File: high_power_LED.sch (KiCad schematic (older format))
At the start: 14 parts

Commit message: Annotate sheets and assign symbols
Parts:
- removed J?: TH-, symbol Connector:Conn_01x01_Female
- D2, D3, D4: renamed from D?; footprint (none) -> extraFootprints:Cree-XLamp-MX6
- H3, H4: renamed from H?; footprint (none) -> MountingHole:MountingHole_2.7mm_M2.5_ISO14580
- HS1: renamed from HS?; footprint (none) -> Heatsink:Heatsink_AAVID_573300D00010G_TO-263
- J15, J16: renamed from J?; footprint (none) -> Connector_PinHeader_2.54mm:PinHeader_1x01_P2.54mm_Vertical
- J17: renamed from J?; value TH+ -> TH; footprint (none) -> Connector_Molex:Molex_PicoBlade_53047-0210_1x02_P1.25mm_Vertical; symbol Connector:Conn_01x01_Female -> Connector:Conn_01x02_Female
- JP3, JP4, JP5: renamed from JP?; footprint (none) -> Jumper:SolderJumper-2_P1.3mm_Open_TrianglePad1.0x1.5mm
- TH1: renamed from TH?; footprint (none) -> Resistor_SMD:R_0603_1608Metric
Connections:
- net at TH1.2: now also J17.2 (Pin_2)
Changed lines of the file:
@@
 $EndDescr
 $Comp
-L Device:LED_PAD D?
+L Device:LED_PAD D2
 U 1 1 602B1BC1
 P 4450 2350
-F 0 "D?" V 4496 2493 50  0000 L CNN
+F 0 "D2" V 4496 2493 50  0000 L CNN
 F 1 "LED_PAD" V 4350 2450 50  0000 L CNN
-F 2 "" H 4450 2350 50  0001 C CNN
+F 2 "extraFootprints:Cree-XLamp-MX6" H 4450 2350 50  0001 C CNN
 F 3 "~" H 4450 2350 50  0001 C CNN
 	1    4450 2350
@@
 $EndComp
 $Comp
-L Device:LED_PAD D?
+L Device:LED_PAD D3
 U 1 1 602B2FF1
 P 4450 2750
-F 0 "D?" V 4496 2893 50  0000 L CNN
+F 0 "D3" V 4496 2893 50  0000 L CNN
 F 1 "LED_PAD" V 4350 2850 50  0000 L CNN
-F 2 "" H 4450 2750 50  0001 C CNN
+F 2 "extraFootprints:Cree-XLamp-MX6" H 4450 2750 50  0001 C CNN
 F 3 "~" H 4450 2750 50  0001 C CNN
 	1    4450 2750
@@
 $EndComp
 $Comp
-L Device:LED_PAD D?
+L Device:LED_PAD D4
 U 1 1 602B35BF
 P 4450 3150
-F 0 "D?" V 4496 3293 50  0000 L CNN
+F 0 "D4" V 4496 3293 50  0000 L CNN
 F 1 "LED_PAD" V 4350 3250 50  0000 L CNN
-F 2 "" H 4450 3150 50  0001 C CNN
+F 2 "extraFootprints:Cree-XLamp-MX6" H 4450 3150 50  0001 C CNN
 F 3 "~" H 4450 3150 50  0001 C CNN
 	1    4450 3150
@@
 $EndComp
 $Comp
-L Jumper:SolderJumper_2_Open JP?
+L Jumper:SolderJumper_2_Open JP4
 U 1 1 602B419C
 P 3850 2750
-F 0 "JP?" V 3850 2662 50  0000 R CNN
+F 0 "JP4" V 3850 2662 50  0000 R CNN
 F 1 "SolderJumper_2_Open" V 3895 2662 50  0001 R CNN
-F 2 "" H 3850 2750 50  0001 C CNN
+F 2 "Jumper:SolderJumper-2_P1.3mm_Open_TrianglePad1.0x1.5mm" H 3850 2750 50  0001 C CNN
 F 3 "~" H 3850 2750 50  0001 C CNN
 	1    3850 2750
@@
 $EndComp
 $Comp
-L Jumper:SolderJumper_2_Open JP?
+L Jumper:SolderJumper_2_Open JP5
 U 1 1 602B5BED
 P 3850 3150
-F 0 "JP?" V 3850 3062 50  0000 R CNN
+F 0 "JP5" V 3850 3062 50  0000 R CNN
 F 1 "SolderJumper_2_Open" V 3895 3062 50  0001 R CNN
-F 2 "" H 3850 3150 50  0001 C CNN
+F 2 "Jumper:SolderJumper-2_P1.3mm_Open_TrianglePad1.0x1.5mm" H 3850 3150 50  0001 C CNN
 F 3 "~" H 3850 3150 50  0001 C CNN
 	1    3850 3150
@@
 Connection ~ 3850 2950
 $Comp
-L Jumper:SolderJumper_2_Open JP?
+L Jumper:SolderJumper_2_Open JP3
 U 1 1 602B6896
 P 3850 2350
-F 0 "JP?" V 3850 2262 50  0000 R CNN
+F 0 "JP3" V 3850 2262 50  0000 R CNN
 F 1 "SolderJumper_2_Open" V 3895 2262 50  0001 R CNN
-F 2 "" H 3850 2350 50  0001 C CNN
+F 2 "Jumper:SolderJumper-2_P1.3mm_Open_TrianglePad1.0x1.5mm" H 3850 2350 50  0001 C CNN
 F 3 "~" H 3850 2350 50  0001 C CNN
 	1    3850 2350
@@
 you can skip LEDs by soldering it's jumper pad
 $Comp
-L Mechanical:Heatsink_Pad HS?
+L Mechanical:Heatsink_Pad HS1
 U 1 1 602B8592
 P 4850 2600
-F 0 "HS?" H 4991 2639 50  0000 L CNN
+F 0 "HS1" H 4991 2639 50  0000 L CNN
 F 1 "Heatsink_Pad" H 4700 2750 50  0000 L CNN
-F 2 "" H 4862 2550 50  0001 C CNN
+F 2 "Heatsink:Heatsink_AAVID_573300D00010G_TO-263" H 4862 2550 50  0001 C CNN
 F 3 "~" H 4862 2550 50  0001 C CNN
 	1    4850 2600
@@
 Connection ~ 4450 3350
 $Comp
-L Device:Thermistor TH?
+L Device:Thermistor TH1
 U 1 1 602BA374
 P 5500 2250
-F 0 "TH?" H 5605 2296 50  0000 L CNN
+F 0 "TH1" H 5605 2296 50  0000 L CNN
 F 1 "Thermistor" H 5605 2205 50  0000 L CNN
-F 2 "" H 5500 2250 50  0001 C CNN
+F 2 "Resistor_SMD:R_0603_1608Metric" H 5500 2250 50  0001 C CNN
 F 3 "~" H 5500 2250 50  0001 C CNN
 	1    5500 2250
@@
 	4500 2050 4450 2050
 $Comp
-L Connector:Conn_01x01_Female J?
+L Connector:Conn_01x01_Female J15
 U 1 1 602C1EF5
 P 4700 2050
-F 0 "J?" H 4700 2100 50  0000 R CNN
+F 0 "J15" H 4700 2100 50  0000 R CNN
 F 1 "Anode" H 4950 2050 50  0000 R CNN
-F 2 "" H 4700 2050 50  0001 C CNN
+F 2 "Connector_PinHeader_2.54mm:PinHeader_1x01_P2.54mm_Vertical" H 4700 2050 50  0001 C CNN
 F 3 "~" H 4700 2050 50  0001 C CNN
 	1    4700 2050
@@
 $EndComp
 $Comp
-L Connector:Conn_01x01_Female J?
-U 1 1 602C273F
-P 6400 2200
-F 0 "J?" H 6400 2250 50  0000 R CNN
-F 1 "TH+" H 6600 2200 50  0000 R CNN
-F 2 "" H 6400 2200 50  0001 C CNN
-F 3 "~" H 6400 2200 50  0001 C CNN
-	1    6400 2200
-	1    0    0    -1
-$EndComp
-$Comp
-L Connector:Conn_01x01_Female J?
-U 1 1 602C2960
-P 6400 2300
-F 0 "J?" H 6400 2350 50  0000 R CNN
-F 1 "TH-" H 6600 2300 50  0000 R CNN
-F 2 "" H 6400 2300 50  0001 C CNN
-F 3 "~" H 6400 2300 50  0001 C CNN
-	1    6400 2300
-	1    0    0    -1
-$EndComp
-$Comp
-L Connector:Conn_01x01_Female J?
+L Connector:Conn_01x01_Female J16
 U 1 1 602C2C18
 P 4700 3450
-F 0 "J?" H 4700 3500 50  0000 R CNN
+F 0 "J16" H 4700 3500 50  0000 R CNN
 F 1 "Cathode" H 5050 3450 50  0000 R CNN
-F 2 "" H 4700 3450 50  0001 C CNN
+F 2 "Connector_PinHeader_2.54mm:PinHeader_1x01_P2.54mm_Vertical" H 4700 3450 50  0001 C CNN
 F 3 "~" H 4700 3450 50  0001 C CNN
 	1    4700 3450
@@
 $EndComp
 $Comp
-L Mechanical:MountingHole H?
+L Mechanical:MountingHole H3
 U 1 1 602C46DF
 P 3000 2100
-F 0 "H?" H 3100 2146 50  0000 L CNN
+F 0 "H3" H 3100 2146 50  0000 L CNN
 F 1 "MountingHole" H 3100 2055 50  0000 L CNN
-F 2 "" H 3000 2100 50  0001 C CNN
+F 2 "MountingHole:MountingHole_2.7mm_M2.5_ISO14580" H 3000 2100 50  0001 C CNN
 F 3 "~" H 3000 2100 50  0001 C CNN
 	1    3000 2100
@@
 $EndComp
 $Comp
-L Mechanical:MountingHole H?
+L Mechanical:MountingHole H4
 U 1 1 602C4749
 P 3000 2350
-F 0 "H?" H 3100 2396 50  0000 L CNN
+F 0 "H4" H 3100 2396 50  0000 L CNN
 F 1 "MountingHole" H 3100 2305 50  0000 L CNN
-F 2 "" H 3000 2350 50  0001 C CNN
+F 2 "MountingHole:MountingHole_2.7mm_M2.5_ISO14580" H 3000 2350 50  0001 C CNN
 F 3 "~" H 3000 2350 50  0001 C CNN
 	1    3000 2350
@@
 Text Notes 3750 1900 0    50   ~ 0
 high power LED
+$Comp
+L Connector:Conn_01x02_Female J17
+U 1 1 602C273F
+P 6400 2200
+F 0 "J17" H 6450 2300 50  0000 R CNN
+F 1 "TH" H 6550 2150 50  0000 R CNN
+F 2 "Connector_Molex:Molex_PicoBlade_53047-0210_1x02_P1.25mm_Vertical" H 6400 2200 50  0001 C CNN
+F 3 "~" H 6400 2200 50  0001 C CNN
+	1    6400 2200
+	1    0    0    -1
+$EndComp
 $EndSCHEMATC

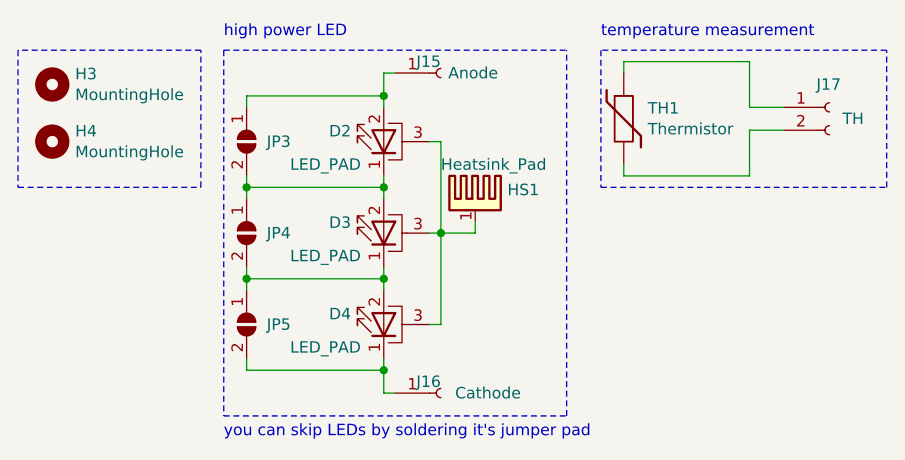
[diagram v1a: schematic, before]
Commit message: Split project into individual projects and reannotate sheets
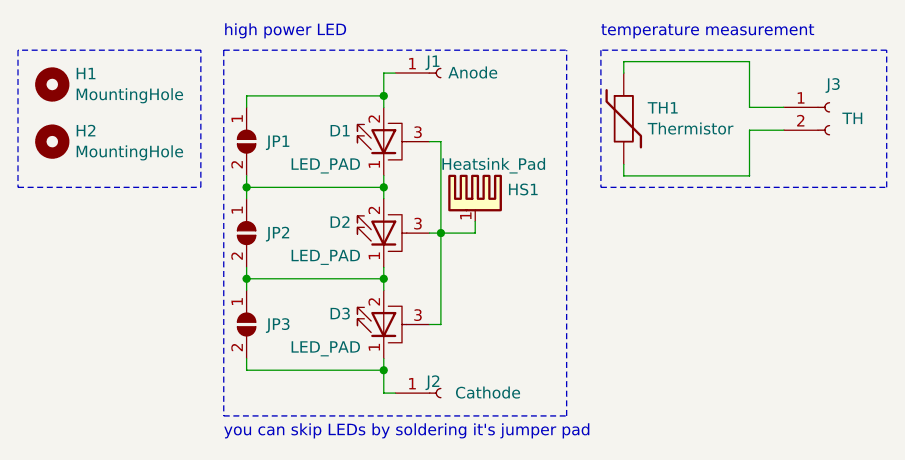
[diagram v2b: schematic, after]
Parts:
- renumbered D2 to D1, D3 to D2, D4 to D3, H3 to H1, H4 to H2, J15 to J1, J16 to J2, J17 to J3, JP3 to JP1, JP4 to JP2, JP5 to JP3
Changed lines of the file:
@@
 $Descr A4 11693 8268
 encoding utf-8
-Sheet 4 4
+Sheet 1 1
 Title ""
 Date ""
@@
 $EndDescr
 $Comp
-L Device:LED_PAD D2
+L Device:LED_PAD D1
 U 1 1 602B1BC1
 P 4450 2350
-F 0 "D2" V 4496 2493 50  0000 L CNN
+F 0 "D1" V 4496 2493 50  0000 L CNN
 F 1 "LED_PAD" V 4350 2450 50  0000 L CNN
 F 2 "extraFootprints:Cree-XLamp-MX6" H 4450 2350 50  0001 C CNN
@@
 $EndComp
 $Comp
-L Device:LED_PAD D3
+L Device:LED_PAD D2
 U 1 1 602B2FF1
 P 4450 2750
-F 0 "D3" V 4496 2893 50  0000 L CNN
+F 0 "D2" V 4496 2893 50  0000 L CNN
 F 1 "LED_PAD" V 4350 2850 50  0000 L CNN
 F 2 "extraFootprints:Cree-XLamp-MX6" H 4450 2750 50  0001 C CNN
@@
 $EndComp
 $Comp
-L Device:LED_PAD D4
+L Device:LED_PAD D3
 U 1 1 602B35BF
 P 4450 3150
-F 0 "D4" V 4496 3293 50  0000 L CNN
+F 0 "D3" V 4496 3293 50  0000 L CNN
 F 1 "LED_PAD" V 4350 3250 50  0000 L CNN
 F 2 "extraFootprints:Cree-XLamp-MX6" H 4450 3150 50  0001 C CNN
@@
 $EndComp
 $Comp
-L Jumper:SolderJumper_2_Open JP4
+L Jumper:SolderJumper_2_Open JP2
 U 1 1 602B419C
 P 3850 2750
-F 0 "JP4" V 3850 2662 50  0000 R CNN
+F 0 "JP2" V 3850 2662 50  0000 R CNN
 F 1 "SolderJumper_2_Open" V 3895 2662 50  0001 R CNN
 F 2 "Jumper:SolderJumper-2_P1.3mm_Open_TrianglePad1.0x1.5mm" H 3850 2750 50  0001 C CNN
@@
 $EndComp
 $Comp
-L Jumper:SolderJumper_2_Open JP5
+L Jumper:SolderJumper_2_Open JP3
 U 1 1 602B5BED
 P 3850 3150
-F 0 "JP5" V 3850 3062 50  0000 R CNN
+F 0 "JP3" V 3850 3062 50  0000 R CNN
 F 1 "SolderJumper_2_Open" V 3895 3062 50  0001 R CNN
 F 2 "Jumper:SolderJumper-2_P1.3mm_Open_TrianglePad1.0x1.5mm" H 3850 3150 50  0001 C CNN
@@
 Connection ~ 3850 2950
 $Comp
-L Jumper:SolderJumper_2_Open JP3
+L Jumper:SolderJumper_2_Open JP1
 U 1 1 602B6896
 P 3850 2350
-F 0 "JP3" V 3850 2262 50  0000 R CNN
+F 0 "JP1" V 3850 2262 50  0000 R CNN
 F 1 "SolderJumper_2_Open" V 3895 2262 50  0001 R CNN
 F 2 "Jumper:SolderJumper-2_P1.3mm_Open_TrianglePad1.0x1.5mm" H 3850 2350 50  0001 C CNN
@@
 	4500 2050 4450 2050
 $Comp
-L Connector:Conn_01x01_Female J15
+L Connector:Conn_01x01_Female J1
 U 1 1 602C1EF5
 P 4700 2050
-F 0 "J15" H 4700 2100 50  0000 R CNN
+F 0 "J1" H 4700 2100 50  0000 R CNN
 F 1 "Anode" H 4950 2050 50  0000 R CNN
 F 2 "Connector_PinHeader_2.54mm:PinHeader_1x01_P2.54mm_Vertical" H 4700 2050 50  0001 C CNN
@@
 $EndComp
 $Comp
-L Connector:Conn_01x01_Female J16
+L Connector:Conn_01x01_Female J2
 U 1 1 602C2C18
 P 4700 3450
-F 0 "J16" H 4700 3500 50  0000 R CNN
+F 0 "J2" H 4700 3500 50  0000 R CNN
 F 1 "Cathode" H 5050 3450 50  0000 R CNN
 F 2 "Connector_PinHeader_2.54mm:PinHeader_1x01_P2.54mm_Vertical" H 4700 3450 50  0001 C CNN
@@
 $EndComp
 $Comp
-L Mechanical:MountingHole H3
+L Mechanical:MountingHole H1
 U 1 1 602C46DF
 P 3000 2100
-F 0 "H3" H 3100 2146 50  0000 L CNN
+F 0 "H1" H 3100 2146 50  0000 L CNN
 F 1 "MountingHole" H 3100 2055 50  0000 L CNN
 F 2 "MountingHole:MountingHole_2.7mm_M2.5_ISO14580" H 3000 2100 50  0001 C CNN
@@
 $EndComp
 $Comp
-L Mechanical:MountingHole H4
+L Mechanical:MountingHole H2
 U 1 1 602C4749
 P 3000 2350
-F 0 "H4" H 3100 2396 50  0000 L CNN
+F 0 "H2" H 3100 2396 50  0000 L CNN
 F 1 "MountingHole" H 3100 2305 50  0000 L CNN
 F 2 "MountingHole:MountingHole_2.7mm_M2.5_ISO14580" H 3000 2350 50  0001 C CNN
@@
 high power LED
 $Comp
-L Connector:Conn_01x02_Female J17
+L Connector:Conn_01x02_Female J3
 U 1 1 602C273F
 P 6400 2200
-F 0 "J17" H 6450 2300 50  0000 R CNN
+F 0 "J3" H 6450 2300 50  0000 R CNN
 F 1 "TH" H 6550 2150 50  0000 R CNN
 F 2 "Connector_Molex:Molex_PicoBlade_53047-0210_1x02_P1.25mm_Vertical" H 6400 2200 50  0001 C CNN

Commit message: Finish high power led pcb
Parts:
- removed J2: Cathode, Connector_PinHeader_2.54mm:PinHeader_1x01_P2.54mm_Vertical, symbol Connector:Conn_01x01_Female
- J1: value Anode -> LED; footprint Connector_PinHeader_2.54mm:PinHeader_1x01_P2.54mm_Vertical -> Connector_PinHeader_2.54mm:PinHeader_1x02_P2.54mm_Vertical; symbol Connector:Conn_01x01_Female -> Connector:Conn_01x02_Female
- renumbered J3 to J2
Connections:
- net Anode: now reaches D1.2 (A), J1.1 (Pin_1), JP1.1 (A)
- net Cathode: now reaches D3.1 (K), JP3.2 (B)
- net Cathode: now also J1.2 (Pin_2)
- net TH+: now reaches J2.1 (Pin_1), TH1.1
- net TH-: now reaches J2.2 (Pin_2), TH1.2
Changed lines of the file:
@@
 $EndComp
-Wire Wire Line
-	4450 3450 4500 3450
 Wire Wire Line
 	5500 2450 5500 2500
@@
 	4500 2050 4450 2050
 $Comp
-L Connector:Conn_01x01_Female J1
+L Connector:Conn_01x02_Female J1
 U 1 1 602C1EF5
-P 4700 2050
-F 0 "J1" H 4700 2100 50  0000 R CNN
-F 1 "Anode" H 4950 2050 50  0000 R CNN
-F 2 "Connector_PinHeader_2.54mm:PinHeader_1x01_P2.54mm_Vertical" H 4700 2050 50  0001 C CNN
-F 3 "~" H 4700 2050 50  0001 C CNN
-	1    4700 2050
-	1    0    0    -1
-$EndComp
-$Comp
-L Connector:Conn_01x01_Female J2
-U 1 1 602C2C18
-P 4700 3450
-F 0 "J2" H 4700 3500 50  0000 R CNN
-F 1 "Cathode" H 5050 3450 50  0000 R CNN
-F 2 "Connector_PinHeader_2.54mm:PinHeader_1x01_P2.54mm_Vertical" H 4700 3450 50  0001 C CNN
-F 3 "~" H 4700 3450 50  0001 C CNN
-	1    4700 3450
+P 5100 3350
+F 0 "J1" H 5100 3400 50  0000 R CNN
+F 1 "LED" V 5200 3350 50  0000 R CNN
+F 2 "Connector_PinHeader_2.54mm:PinHeader_1x02_P2.54mm_Vertical" H 5100 3350 50  0001 C CNN
+F 3 "~" H 5100 3350 50  0001 C CNN
+	1    5100 3350
 	1    0    0    -1
 $EndComp
@@
 high power LED
 $Comp
-L Connector:Conn_01x02_Female J3
+L Connector:Conn_01x02_Female J2
 U 1 1 602C273F
 P 6400 2200
-F 0 "J3" H 6450 2300 50  0000 R CNN
+F 0 "J2" H 6450 2300 50  0000 R CNN
 F 1 "TH" H 6550 2150 50  0000 R CNN
 F 2 "Connector_Molex:Molex_PicoBlade_53047-0210_1x02_P1.25mm_Vertical" H 6400 2200 50  0001 C CNN
@@
 	1    0    0    -1
 $EndComp
+Text Label 4500 2050 0    50   ~ 0
+Anode
+Text Label 4850 3450 2    50   ~ 0
+Cathode
+Wire Wire Line
+	4450 3450 4900 3450
+Wire Wire Line
+	4900 3350 4850 3350
+Text Label 4850 3350 2    50   ~ 0
+Anode
+Text Label 6050 2200 0    50   ~ 0
+TH+
+Text Label 6050 2300 0    50   ~ 0
+TH-
 $EndSCHEMATC
